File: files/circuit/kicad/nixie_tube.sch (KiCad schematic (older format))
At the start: 16 parts, among them K1 CONN_3, K2 CONN_3, K3 CONN_3, K4 CONN_3, U1 NEON, U10 NIXIE_IN_16, U2 NEON, U3 NEON, U4 NEON, U5 NIXIE_IN_16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

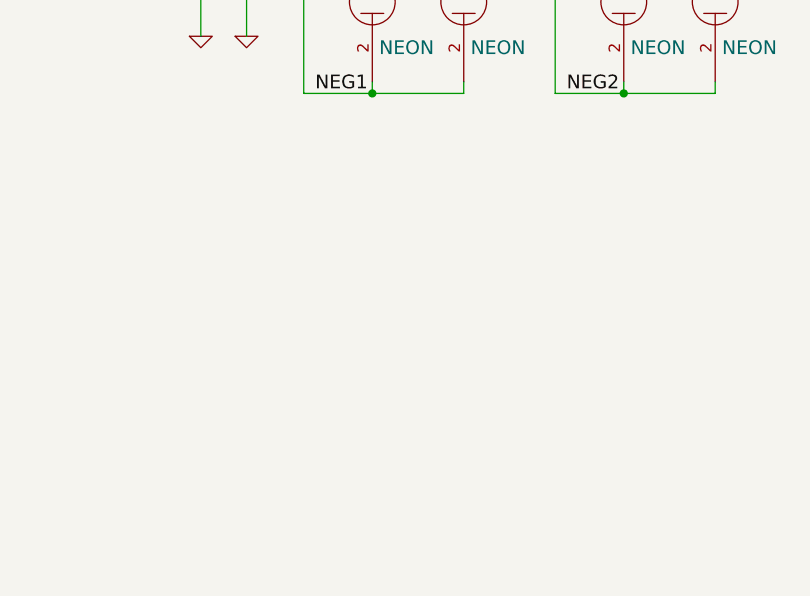
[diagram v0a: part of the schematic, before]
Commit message: 回路完成、ディレクトリ構造変更
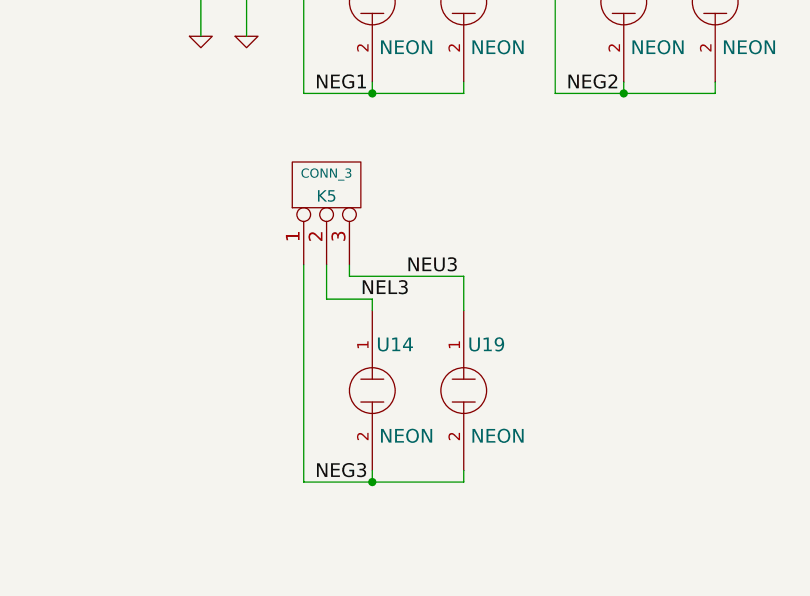
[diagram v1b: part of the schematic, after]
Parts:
- added K5: CONN_3, ~, symbol CONN_3
- added U14, U19: NEON, symbol NEON
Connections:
- new net NEG3: K5.1 (P1), U14.2, U19.2
- new net NEL3: K5.2 (PM), U14.1
- new net NEU3: K5.3 (P3), U19.1
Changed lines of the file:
@@
 Sheet 3 8
 Title ""
-Date "6 sep 2014"
+Date "7 sep 2014"
 Rev ""
 Comp ""
@@
 Text Label 3700 3950 0    60   ~ 0
 NEU1
+$Comp
+L NEON U14
+U 1 1 540C8497
+P 3550 6150
+F 0 "U14" H 3650 6350 60  0000 C CNN
+F 1 "NEON" H 3700 5950 60  0000 C CNN
+F 2 "" H 3650 6350 60  0000 C CNN
+F 3 "" H 3650 6350 60  0000 C CNN
+	1    3550 6150
+	1    0    0    -1
+$EndComp
+$Comp
+L NEON U19
+U 1 1 540C849D
+P 3950 6150
+F 0 "U19" H 4050 6350 60  0000 C CNN
+F 1 "NEON" H 4100 5950 60  0000 C CNN
+F 2 "" H 4050 6350 60  0000 C CNN
+F 3 "" H 4050 6350 60  0000 C CNN
+	1    3950 6150
+	1    0    0    -1
+$EndComp
+$Comp
+L CONN_3 K5
+U 1 1 540C84A3
+P 3350 5250
+F 0 "K5" V 3300 5250 50  0000 C CNN
+F 1 "CONN_3" V 3400 5250 40  0000 C CNN
+F 2 "~" H 3350 5250 60  0000 C CNN
+F 3 "~" H 3350 5250 60  0000 C CNN
+	1    3350 5250
+	0    -1   -1   0
+$EndComp
+Wire Wire Line
+	3950 5650 3950 5800
+Wire Wire Line
+	3550 6500 3550 6500
+Wire Wire Line
+	3950 6500 3950 6500
+Wire Wire Line
+	3950 6550 3950 6500
+Wire Wire Line
+	3250 6550 3950 6550
+Wire Wire Line
+	3550 6500 3550 6550
+Connection ~ 3550 6550
+Wire Wire Line
+	3550 5800 3550 5750
+Wire Wire Line
+	3550 5750 3350 5750
+Wire Wire Line
+	3350 5750 3350 5600
+Wire Wire Line
+	3450 5600 3450 5650
+Wire Wire Line
+	3450 5650 3950 5650
+Wire Wire Line
+	3250 6550 3250 5600
+Text Label 3300 6550 0    60   ~ 0
+NEG3
+Text Label 3500 5750 0    60   ~ 0
+NEL3
+Text Label 3700 5650 0    60   ~ 0
+NEU3
 $EndSCHEMATC

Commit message: 基板完成、発注版
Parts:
- renumbered U10 to NI1, U7 to NI2, U9 to NI3, U6 to NI4, U8 to NI5, U5 to NI6
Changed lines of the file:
@@
 Sheet 3 8
 Title ""
-Date "7 sep 2014"
+Date "8 sep 2014"
 Rev ""
 Comp ""
@@
 $EndDescr
 $Comp
-L NIXIE_IN_16 U10
+L NIXIE_IN_16 NI1
 U 1 1 53F9F8E3
 P 9250 5850
-F 0 "U10" H 9450 6100 60  0000 C CNN
+F 0 "NI1" H 9450 6100 60  0000 C CNN
 F 1 "NIXIE_IN_16" H 8900 6100 60  0000 C CNN
 F 2 "" H 9250 5950 60  0000 C CNN
@@
 	8600 6650 8700 6550
 $Comp
-L NIXIE_IN_16 U7
+L NIXIE_IN_16 NI2
 U 1 1 53F9F901
 P 7550 5850
-F 0 "U7" H 7750 6100 60  0000 C CNN
+F 0 "NI2" H 7750 6100 60  0000 C CNN
 F 1 "NIXIE_IN_16" H 7200 6100 60  0000 C CNN
 F 2 "" H 7550 5950 60  0000 C CNN
@@
 	6900 6650 7000 6550
 $Comp
-L NIXIE_IN_16 U9
+L NIXIE_IN_16 NI3
 U 1 1 53F9F91F
 P 9250 3750
-F 0 "U9" H 9450 4000 60  0000 C CNN
+F 0 "NI3" H 9450 4000 60  0000 C CNN
 F 1 "NIXIE_IN_16" H 8900 4000 60  0000 C CNN
 F 2 "" H 9250 3850 60  0000 C CNN
@@
 	8600 4550 8700 4450
 $Comp
-L NIXIE_IN_16 U6
+L NIXIE_IN_16 NI4
 U 1 1 53F9F93D
 P 7550 3750
-F 0 "U6" H 7750 4000 60  0000 C CNN
+F 0 "NI4" H 7750 4000 60  0000 C CNN
 F 1 "NIXIE_IN_16" H 7200 4000 60  0000 C CNN
 F 2 "" H 7550 3850 60  0000 C CNN
@@
 	6900 4550 7000 4450
 $Comp
-L NIXIE_IN_16 U8
+L NIXIE_IN_16 NI5
 U 1 1 53F9F95B
 P 9200 1500
-F 0 "U8" H 9400 1750 60  0000 C CNN
+F 0 "NI5" H 9400 1750 60  0000 C CNN
 F 1 "NIXIE_IN_16" H 8850 1750 60  0000 C CNN
 F 2 "" H 9200 1600 60  0000 C CNN
@@
 	8550 2300 8650 2200
 $Comp
-L NIXIE_IN_16 U5
+L NIXIE_IN_16 NI6
 U 1 1 53F9F979
 P 7500 1500
-F 0 "U5" H 7700 1750 60  0000 C CNN
+F 0 "NI6" H 7700 1750 60  0000 C CNN
 F 1 "NIXIE_IN_16" H 7150 1750 60  0000 C CNN
 F 2 "" H 7500 1600 60  0000 C CNN
